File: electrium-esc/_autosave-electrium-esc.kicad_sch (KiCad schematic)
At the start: 0 parts

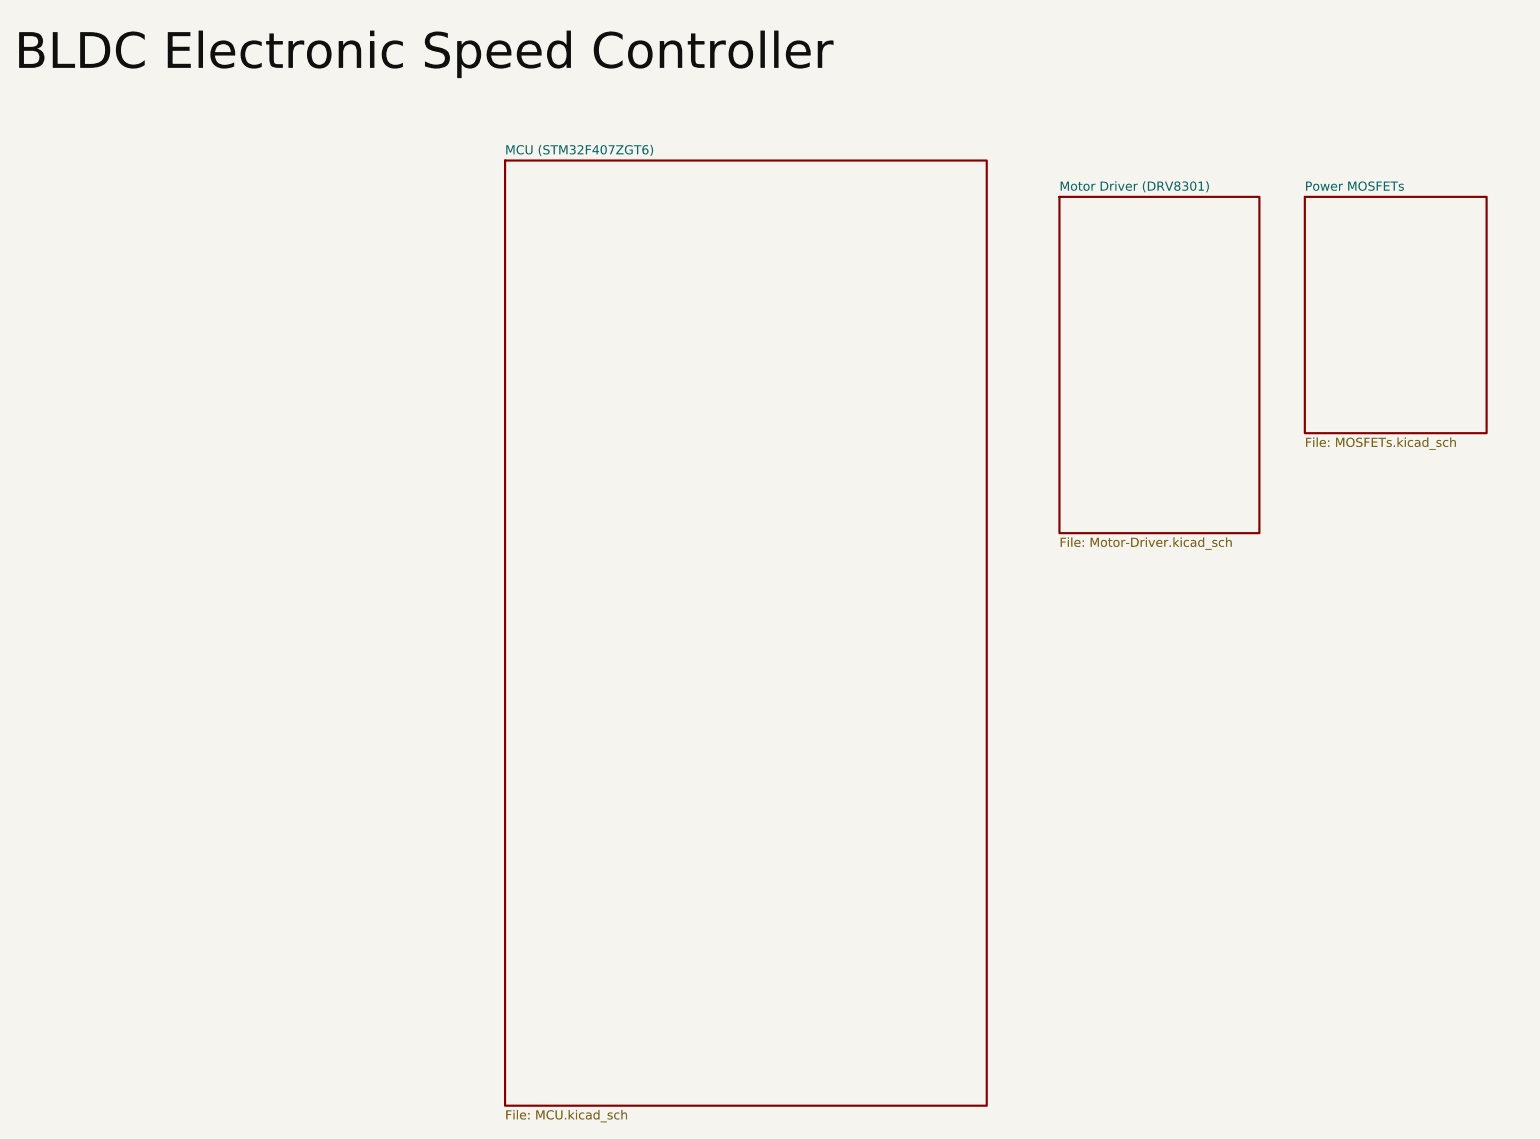
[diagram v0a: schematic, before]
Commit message: Add further connections to MCU
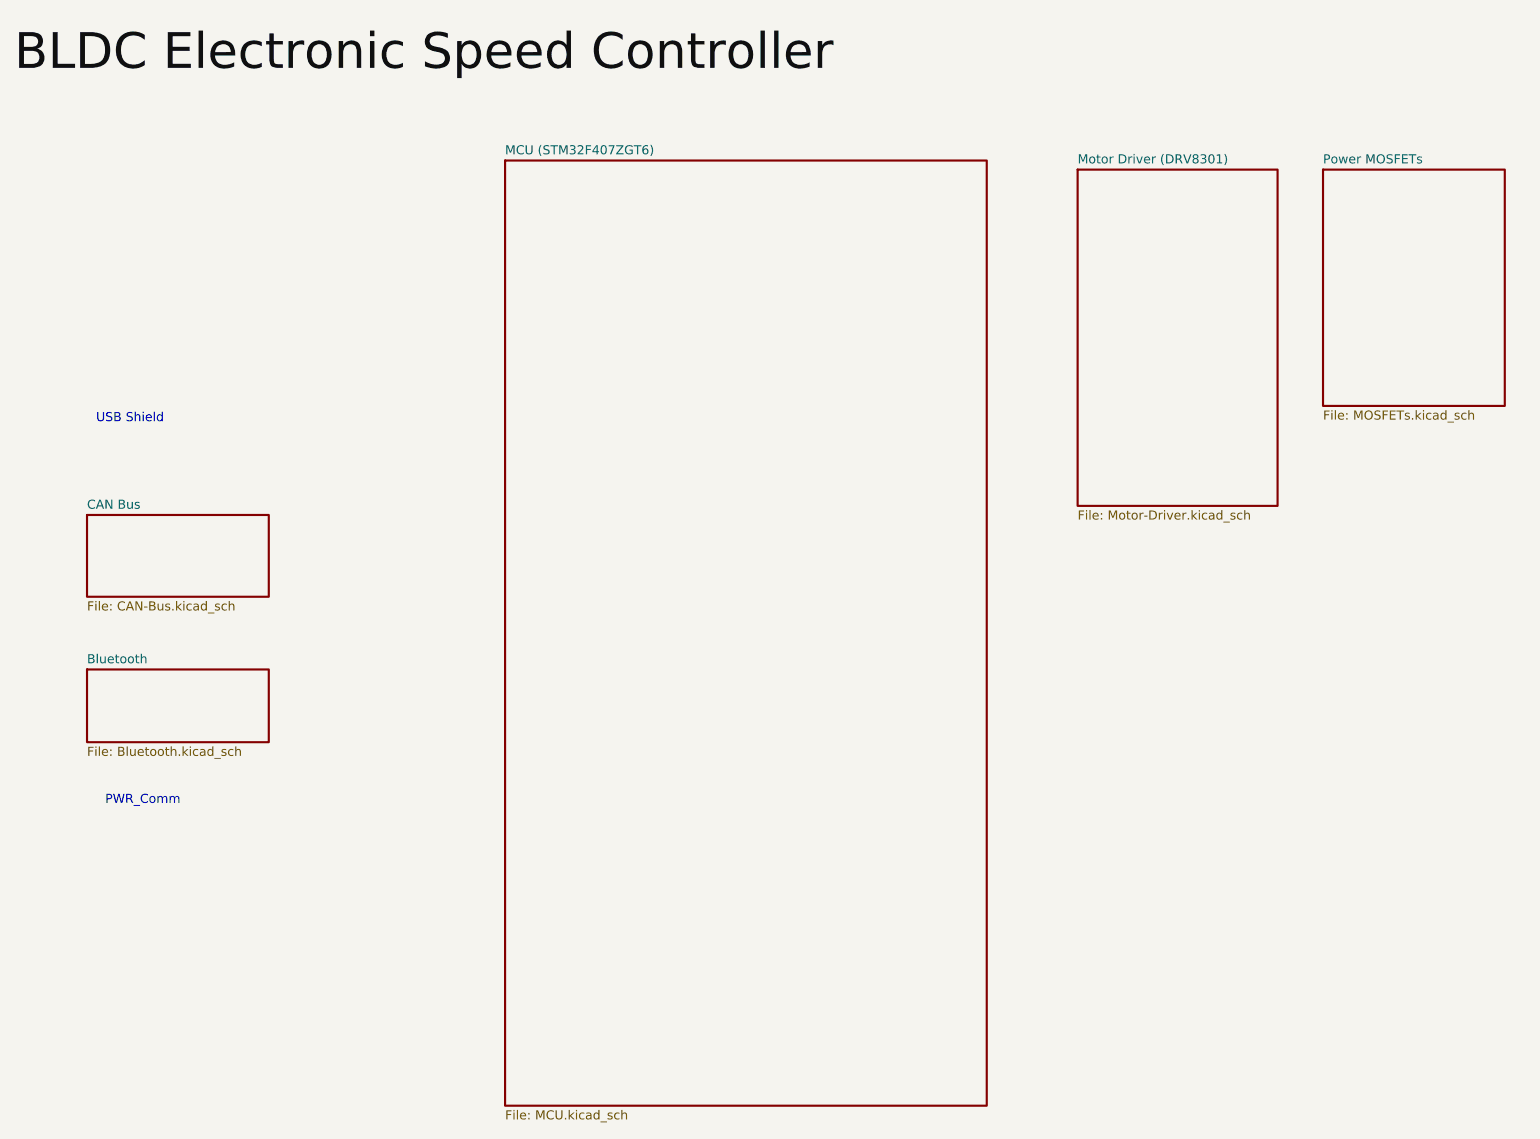
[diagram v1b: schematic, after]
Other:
- added sheet Bluetooth (Bluetooth.kicad_sch)
- added sheet CAN Bus (CAN-Bus.kicad_sch)
- note added: "PWR_Comm"
- note added: "USB Shield"
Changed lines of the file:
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@@
     (comment 1 "Top Level")
+  )
+  (text "PWR_Comm\n" (at 31.75 128.27 0)
+    (effects (font (size 1.27 1.27)) (justify left bottom))
+  )
+  (text "USB Shield\n" (at 30.48 74.93 0)
+    (effects (font (size 1.27 1.27)) (justify left bottom))
   )
   (label "BLDC Electronic Speed Controller" (at 19.05 26.67 0)
     (effects (font (size 5 5)) (justify left bottom))
   )
-  (sheet (at 165.1 43.18) (size 27.94 46.99) (fields_autoplaced)
+  (sheet (at 167.64 39.37) (size 27.94 46.99) (fields_autoplaced)
     (stroke (width 0.3) (type solid) (color 0 0 0 0))
     (fill (color 0 0 0 0.0000))
-    (property "Sheet name" "Motor Driver (DRV8301)" (id 0) (at 165.1 42.4684 0)
+    (property "Sheet name" "Motor Driver (DRV8301)" (id 0) (at 167.64 38.6584 0)
       (effects (font (size 1.27 1.27)) (justify left bottom))
     )
-    (property "Sheet file" "Motor-Driver.kicad_sch" (id 1) (at 165.1 90.7546 0)
+    (property "Sheet file" "Motor-Driver.kicad_sch" (id 1) (at 167.64 86.9446 0)
+      (effects (font (size 1.27 1.27)) (justify left top))
+    )
+  )
+  (sheet (at 29.21 109.22) (size 25.4 10.16) (fields_autoplaced)
+    (stroke (width 0.3) (type solid) (color 0 0 0 0))
+    (fill (color 0 0 0 0.0000))
+    (property "Sheet name" "Bluetooth" (id 0) (at 29.21 108.5084 0)
+      (effects (font (size 1.27 1.27)) (justify left bottom))
+    )
+    (property "Sheet file" "Bluetooth.kicad_sch" (id 1) (at 29.21 119.9646 0)
       (effects (font (size 1.27 1.27)) (justify left top))
     )
@@
     )
   )
-  (sheet (at 199.39 43.18) (size 25.4 33.02) (fields_autoplaced)
+  (sheet (at 201.93 39.37) (size 25.4 33.02) (fields_autoplaced)
     (stroke (width 0.3) (type solid) (color 0 0 0 0))
     (fill (color 0 0 0 0.0000))
-    (property "Sheet name" "Power MOSFETs" (id 0) (at 199.39 42.4684 0)
+    (property "Sheet name" "Power MOSFETs" (id 0) (at 201.93 38.6584 0)
       (effects (font (size 1.27 1.27)) (justify left bottom))
     )
-    (property "Sheet file" "MOSFETs.kicad_sch" (id 1) (at 199.39 76.7846 0)
+    (property "Sheet file" "MOSFETs.kicad_sch" (id 1) (at 201.93 72.9746 0)
+      (effects (font (size 1.27 1.27)) (justify left top))
+    )
+  )
+  (sheet (at 29.21 87.63) (size 25.4 11.43) (fields_autoplaced)
+    (stroke (width 0.3) (type solid) (color 0 0 0 0))
+    (fill (color 0 0 0 0.0000))
+    (property "Sheet name" "CAN Bus" (id 0) (at 29.21 86.9184 0)
+      (effects (font (size 1.27 1.27)) (justify left bottom))
+    )
+    (property "Sheet file" "CAN-Bus.kicad_sch" (id 1) (at 29.21 99.6446 0)
       (effects (font (size 1.27 1.27)) (justify left top))
     )
@@
     (path "/4dcd2554-0c0c-4fca-b220-d2fb156d9cf9" (page "3"))
     (path "/9cfb263a-ea56-4cbe-86e2-b1fdf4c95ad6" (page "4"))
+    (path "/f169605c-998e-4bf3-977e-b281c665fab8" (page "5"))
+    (path "/8e3fe61b-a8c8-4119-95ec-c642aa46593a" (page "6"))
   )
   (symbol_instances
@@
     )
     (path "/95515899-f309-4706-b478-ef0c1d74de3d/5edcc7cb-df6a-47ca-9704-c1c2f8fc99a3"
+      (reference "#PWR?") (unit 1) (value "GND") (footprint "")
+    )
+    (path "/95515899-f309-4706-b478-ef0c1d74de3d/67c7ca55-4024-4176-80f1-198aced55fbe"
       (reference "#PWR?") (unit 1) (value "GND") (footprint "")
     )
@@
       (reference "C?") (unit 1) (value "100n") (footprint "")
     )
+    (path "/95515899-f309-4706-b478-ef0c1d74de3d/dafbf49e-57ab-4108-ba3a-ab69efabd1d0"
+      (reference "C?") (unit 1) (value "27p") (footprint "")
+    )
     (path "/95515899-f309-4706-b478-ef0c1d74de3d/def6c557-9378-4335-92be-4e0ff8388a8d"
       (reference "C?") (unit 1) (value "100n") (footprint "")
@@
       (reference "C?") (unit 1) (value "100n") (footprint "")
     )
+    (path "/95515899-f309-4706-b478-ef0c1d74de3d/f90913ed-7a2c-4c5e-9f76-5351103d08bf"
+      (reference "C?") (unit 1) (value "27p") (footprint "")
+    )
     (path "/95515899-f309-4706-b478-ef0c1d74de3d/3e6c1971-6bbc-4023-a5ae-394bc3e11e8b"
